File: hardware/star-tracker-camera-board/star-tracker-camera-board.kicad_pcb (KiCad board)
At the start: 4 copper layers, 31.5 x 13.6 mm, 41 parts, among them J1 3-1734742-6, U1 AR0134CSSM00SPCA0, U2 TPS70618DRVR, U3 TPS71928-28DRVT, U4 TPS71928-28DRVT, X1 KC2520B27.0000C10E00

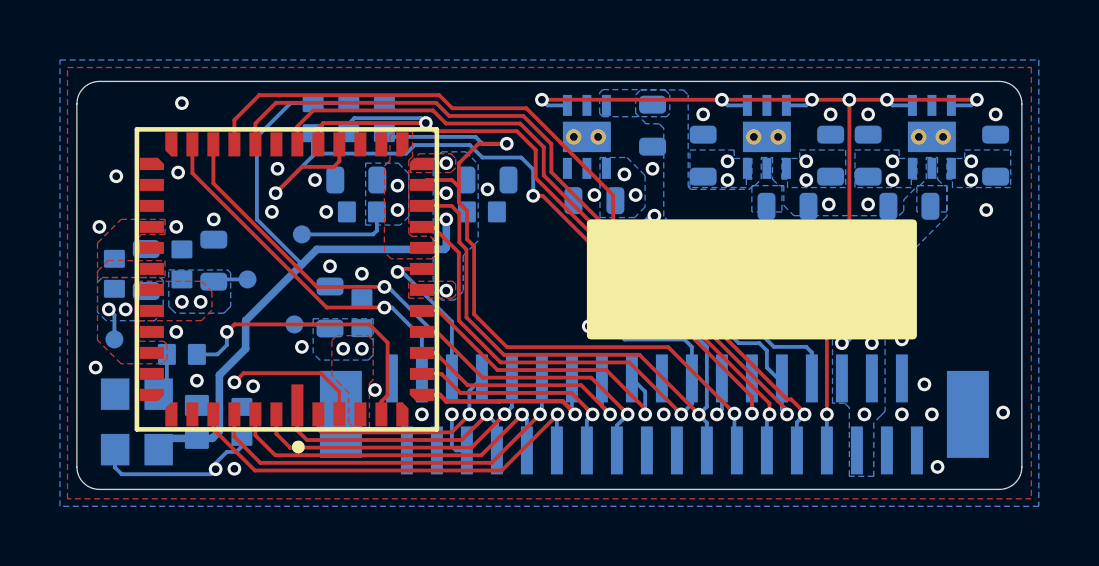
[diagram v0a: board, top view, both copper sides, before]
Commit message: More EAGLE import clean up
Fixed BOM, still needs 0402 passives. Fixed ERCs, and a bunch of DRCs. U1 still needs footprint cleanup.
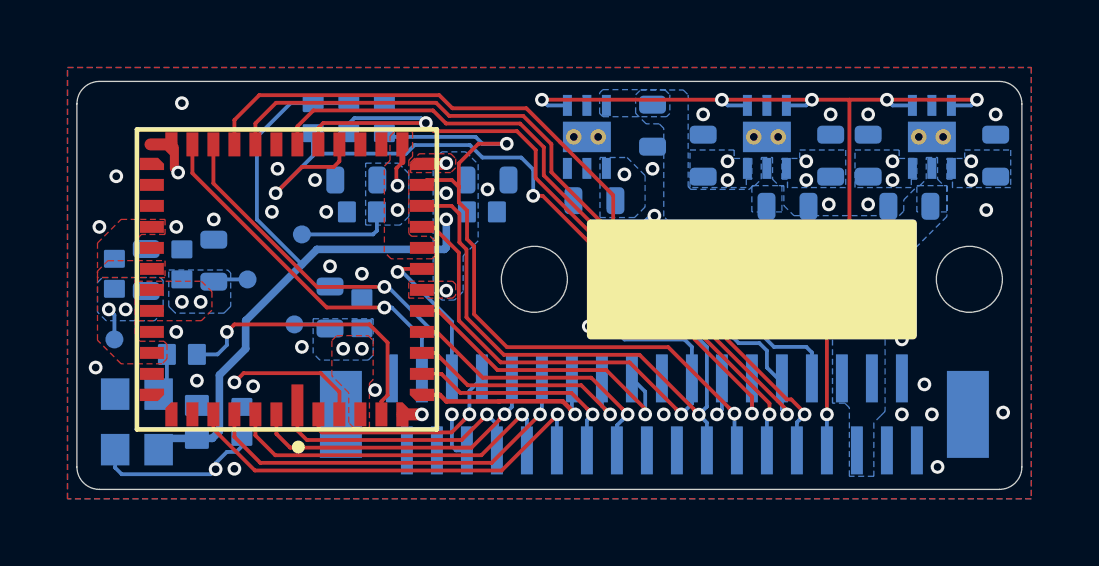
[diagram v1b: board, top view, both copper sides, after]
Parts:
- added REF**: MountingHole_2.2mm_M2, MountingHole:MountingHole_2.2mm_M2, F.Cu at (148.0, 104.8)
- added REF**: MountingHole_2.2mm_M2, MountingHole:MountingHole_2.2mm_M2, F.Cu at (162.5, 104.8)
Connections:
- U1 pad 20: (no net) -> unconnected-(U1-NC-Pad20)
- U1 pad 21: (no net) -> unconnected-(U1-NC-Pad21)
- U1 pad 31: (no net) -> unconnected-(U1-NC-Pad31)
- U1 pad 32: (no net) -> unconnected-(U1-NC-Pad32)
- U1 pad 33: (no net) -> unconnected-(U1-NC-Pad33)
- U1 pad 41: (no net) -> unconnected-(U1-NC-Pad41)
- U1 pad 42: (no net) -> unconnected-(U1-NC-Pad42)
- U1 pad 43: (no net) -> unconnected-(U1-NC-Pad43)
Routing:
- net GND: track 0.00 -> 2.38 mm
- net VDD: track 12.9 -> 14.4 mm, vias 4 -> 3
- net 3.3V: track 2.73 -> 1.50 mm, vias 3 -> 0
- net VDD_IO: track 40.3 -> 41.1 mm
- net /VREG_EN: vias 8 -> 7
- net (no net): vias 1 -> 0
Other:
- board text added: "OCBv${REVISION} OLIVER REW ${ISSUE_DATE}"
- board text removed: "OCBv4 OLIVER REW 2020.10.19"

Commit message: More DRC cleanup. Better now.
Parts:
- U1: value AR0134CSSM00SPCA0 -> Val**
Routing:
- net GND: track 2.38 -> 0.14 mm
- net VDD: track 14.4 -> 12.9 mm
- net VDD_IO: track 41.1 -> 40.4 mm

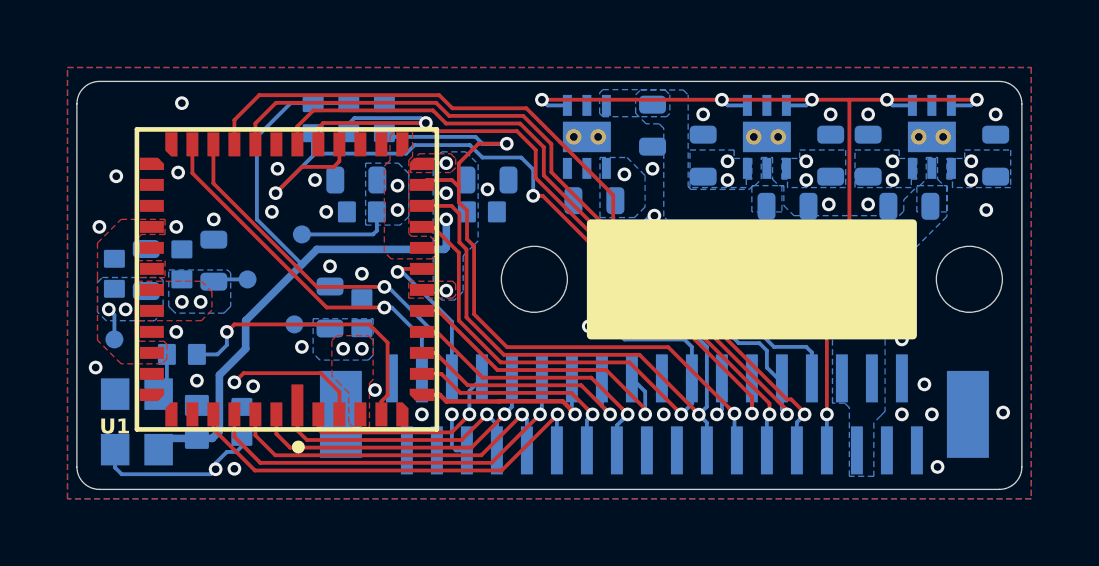
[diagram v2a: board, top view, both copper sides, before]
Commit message: Updated schematic
Updated schematic symbols footprints and replaced EOL osc. Rearranged component designators.
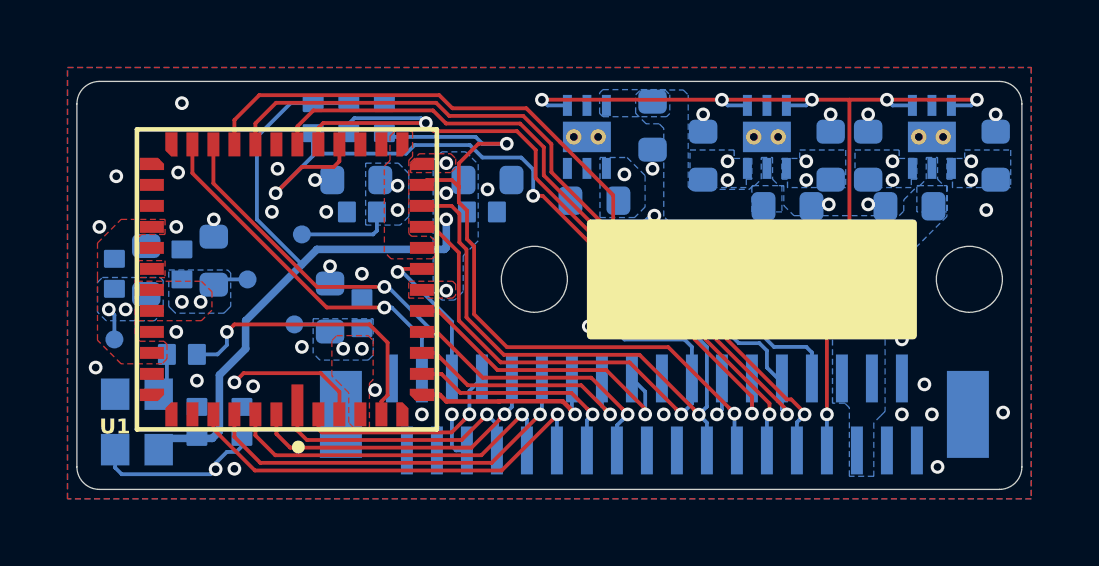
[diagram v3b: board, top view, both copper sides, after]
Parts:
- C1: footprint star-tracker-camera-board:.0402-A-NOSILK -> oresat-passives:0402-B-NOSILK
- C10, C11, C12, C14, C15, C16, C18, C19, C2, C4, C6, C7, C8: footprint star-tracker-camera-board:.0603-C-NOSILK -> oresat-passives:c_0603-SMALL
- C13, C17, C3, C5, C9, R4, R5, R7, R8: footprint star-tracker-camera-board:.0402-B-NOSILK -> oresat-passives:0402-B-NOSILK
- R10, R11, R12, R2, R9: footprint star-tracker-camera-board:.0402-B -> oresat-passives:0402-B-NOSILK
- U1: value Val** -> AR0134CSSM00SPCA0
- X1: value KC2520B27.0000C10E00 -> MC2520Z27.0000C19XSH

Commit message: Fixed library links and updated footprints to the latest.
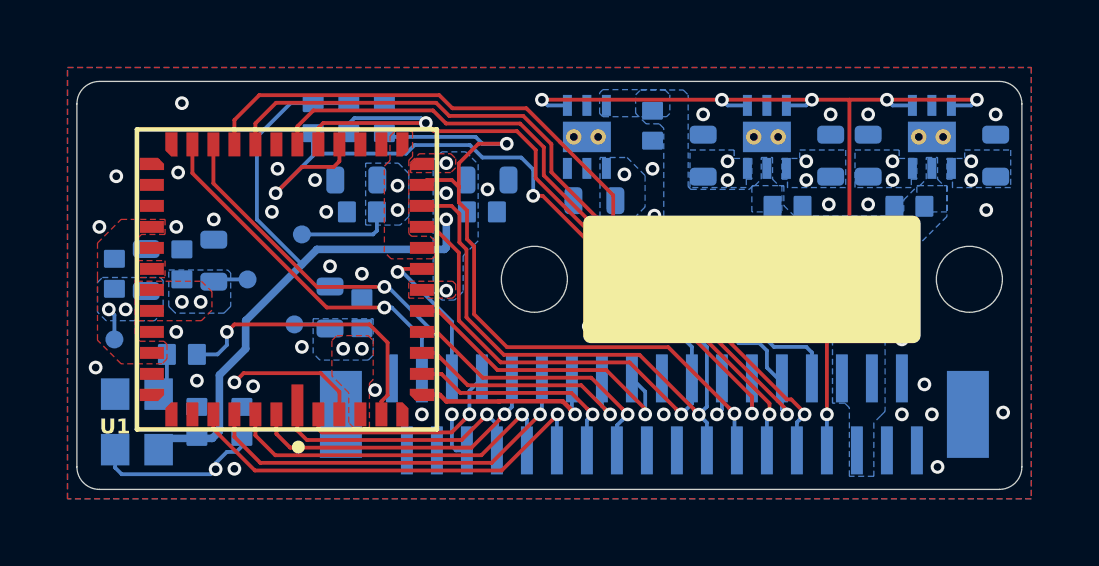
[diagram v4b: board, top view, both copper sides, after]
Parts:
- C10, C14, C6: footprint oresat-passives:c_0603-SMALL -> oresat-passives:0402-B-NOSILK
- C11, C12, C15, C16, C18, C19, C2, C4, C7, C8: footprint oresat-passives:c_0603-SMALL -> oresat-passives:0603-C-NOSILK
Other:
- board text added: "OCB v${REVISION} OR et al ${ISSUE_DATE}"
- board text removed: "OCBv${REVISION} OLIVER REW ${ISSUE_DATE}"
